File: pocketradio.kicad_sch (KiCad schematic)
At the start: 23 parts, among them CN1 PJ-320D, U1 SI4702-C19-GMR, U2 CH32V003F4U6, U3 TPA6130A2RTJR

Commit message: lots of stuff
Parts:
- added BT1: MY-2032-12, easyeda2kicad:BAT-SMD_MY-2032-12, symbol JLCImport:MY-2032-12
- added J1: Conn_01x03_Pin, Connector_PinHeader_2.54mm:PinHeader_1x03_P2.54mm_Vertical, symbol Connector:Conn_01x03_Pin
- added R1, R2, R3, R4: 10k, Resistor_SMD:R_0603_1608Metric, symbol Device:R_Small
- added SW1, SW2, SW3, SW4: SW_Push_45deg, easyeda2kicad:SW-SMD_4P-L4.2-W3.3-P2.15-LS5.1, symbol Switch:SW_Push_45deg
- added SW5: K3-2235S-F1, easyeda2kicad:SW-SMD_MST22D18G2, symbol JLCImport:K3-2235S-F1
- renumbered C4 to C2, C5 to C3, C6 to C4, C7 to C5, C3 to C6, C9 to C7, C2 to C9, R8 to R10, R1 to R5, R2 to R6, R3 to R7, R4 to R8, R7 to R9, U2 to U1, U3 to U2, U1 to U3
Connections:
- net +3V3: now also J1.2 (Pin_2), R1.1, R2.1, R3.1, R4.1, SW5.2, SW5.5
- net GND: now also BT1.2, J1.3 (Pin_3), SW1.2, SW2.2, SW3.2, SW4.2
- net SWDEBUG: now also J1.1 (Pin_1)
- net PD3: now reaches U1.17 (PD3)
- net PD3: now also R2.2, SW2.1
- net PD4: now reaches U1.18 (PD4)
- net PD4: now also R1.2, SW1.1
- net PD5: now reaches U1.19 (PD5)
- net PD5: now also R3.2, SW3.1
- net PD6: now reaches U1.20 (PD6)
- net PD6: now also R4.2, SW4.1
- new net: BT1.1, SW5.3, SW5.6
- no-connect marks 18 -> 16
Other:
- moved on the sheet: C6, OSC1

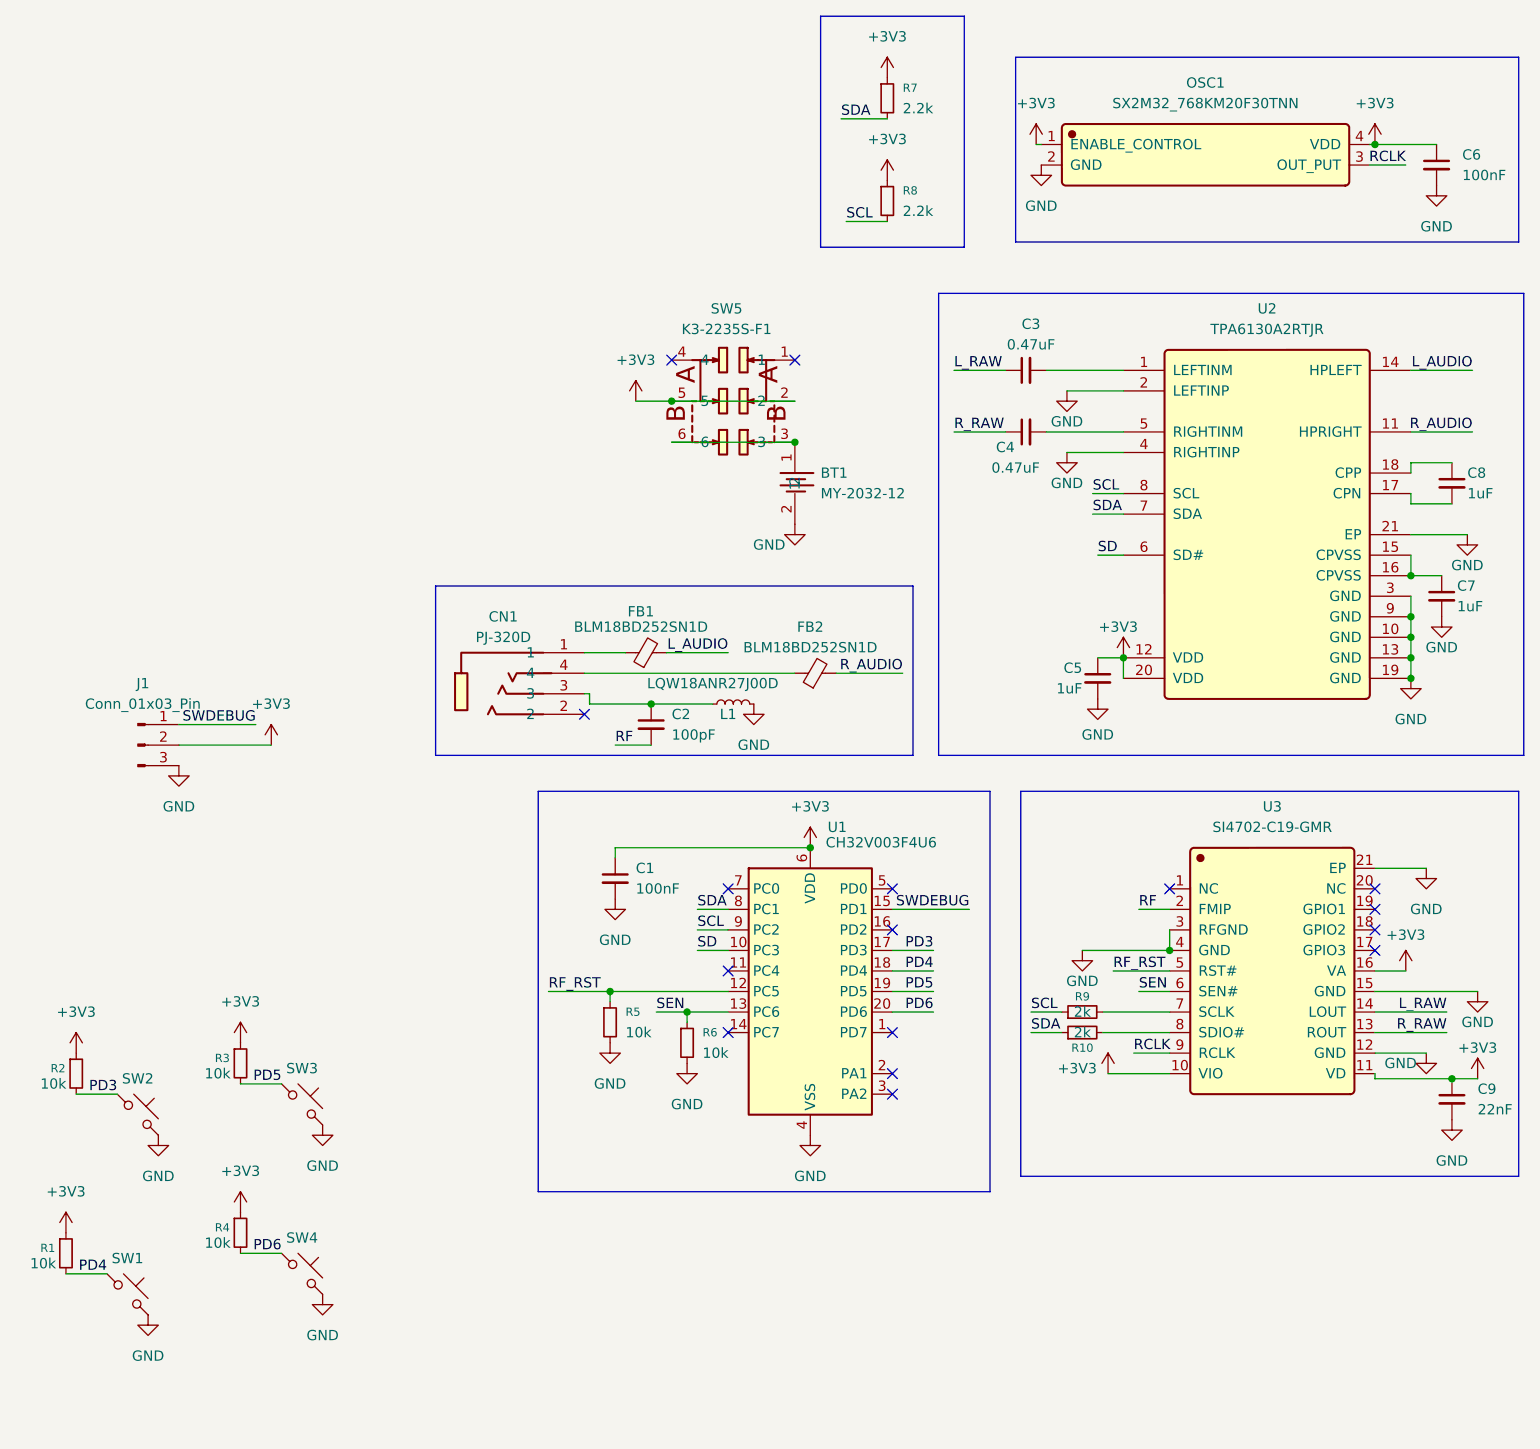
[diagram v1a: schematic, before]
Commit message: power LED
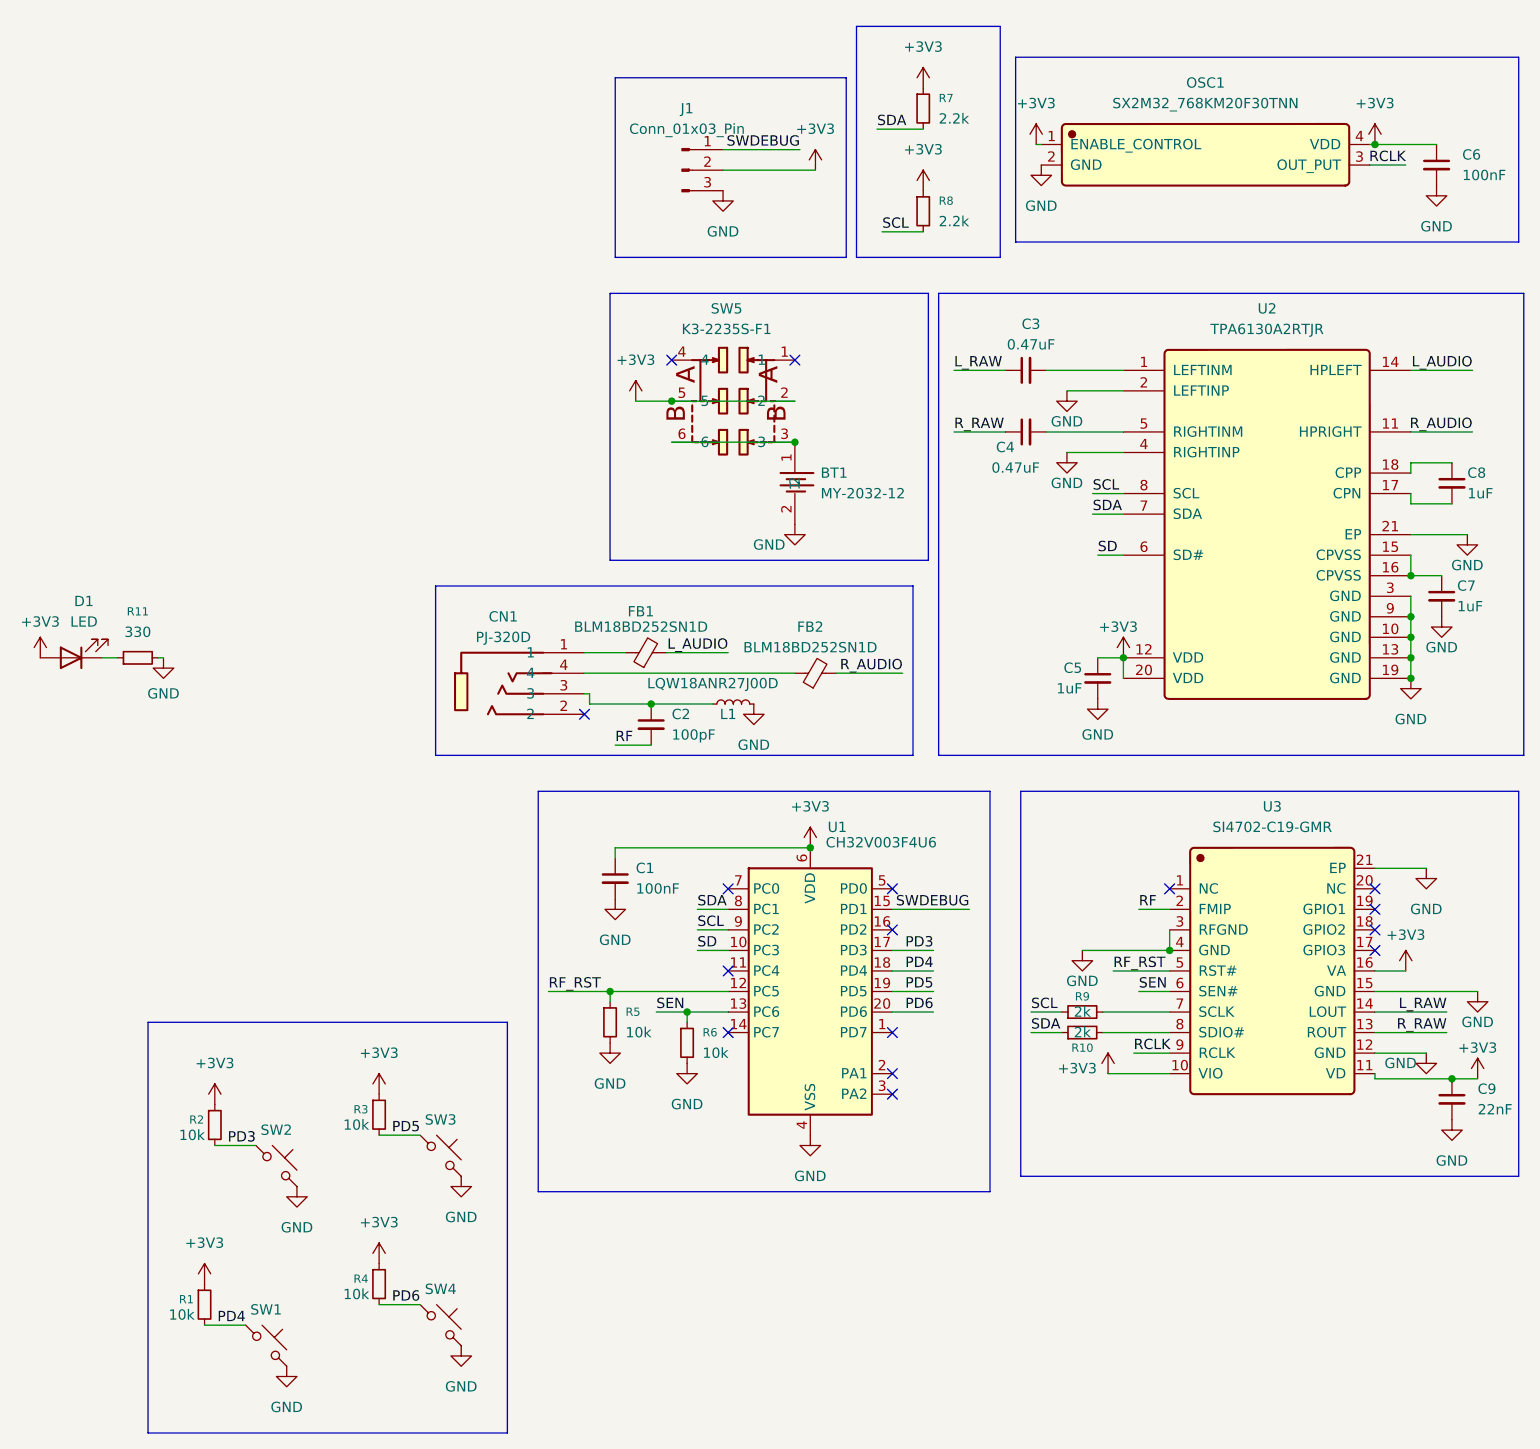
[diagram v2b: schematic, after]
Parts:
- added D1: LED, LED_SMD:LED_0402_1005Metric, symbol Device:LED
- added R11: 330, Resistor_SMD:R_0402_1005Metric, symbol Device:R_Small
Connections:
- net +3V3: now also D1.2 (A)
- net GND: now also R11.2
- new net: D1.1 (K), R11.1
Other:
- moved on the sheet: J1, R1, R2, R3, R4, R7, R8, SW1, SW2, SW3, SW4

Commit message: recheck audio jack pinou
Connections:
- net at C2.1, CN1.3, L1.1: now also CN1.2
- no-connect marks 16 -> 15
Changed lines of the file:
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@@
+	)
+	(junction
+		(at 173.99 102.87)
+		(diameter 0)
+		(color 0 0 0 0)
 	)
 	(junction
@@
 	)
 	(junction
-		(at 173.99 102.87)
+		(at 165.735 102.87)
 		(diameter 0)
 		(color 0 0 0 0)
@@
 	)
 	(no_connect
-		(at 165.735 104.14)
-	)
-	(no_connect
 		(at 263.525 128.27)
 	)
@@
 	(wire
 		(pts
+			(xy 165.735 102.87) (xy 165.735 104.14)
+		)
+		(stroke
+			(width 0)
+			(type default)
+		)
+	)
+	(wire
+		(pts
 			(xy 267.97 84.455) (xy 267.97 86.995)
 		)
@@
 	(wire
 		(pts
-			(xy 166.37 101.6) (xy 165.735 101.6)
-		)
-		(stroke
-			(width 0)
-			(type default)
-		)
-	)
-	(wire
-		(pts
 			(xy 208.915 133.35) (xy 203.835 133.35)
 		)
@@
 	(wire
 		(pts
-			(xy 166.37 102.87) (xy 173.99 102.87)
+			(xy 165.735 102.87) (xy 173.99 102.87)
 		)
 		(stroke
@@
 	(wire
 		(pts
-			(xy 166.37 102.87) (xy 166.37 101.6)
-		)
-		(stroke
+			(xy 165.735 102.87) (xy 165.735 101.6)
+		)
+		(stroke
